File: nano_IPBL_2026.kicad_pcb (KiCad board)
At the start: 2 copper layers, 44 x 85 mm, 21 parts, among them J1 DB301V-5.0-2P, M1 Motor_Servo, M10 Motor_Servo, M11 Motor_Servo, M12 Motor_Servo, M2 Motor_Servo, M3 Motor_Servo, M4 Motor_Servo, M5 Motor_Servo, M6 Motor_Servo, M7 Motor_Servo, M8 Motor_Servo, M9 Motor_Servo

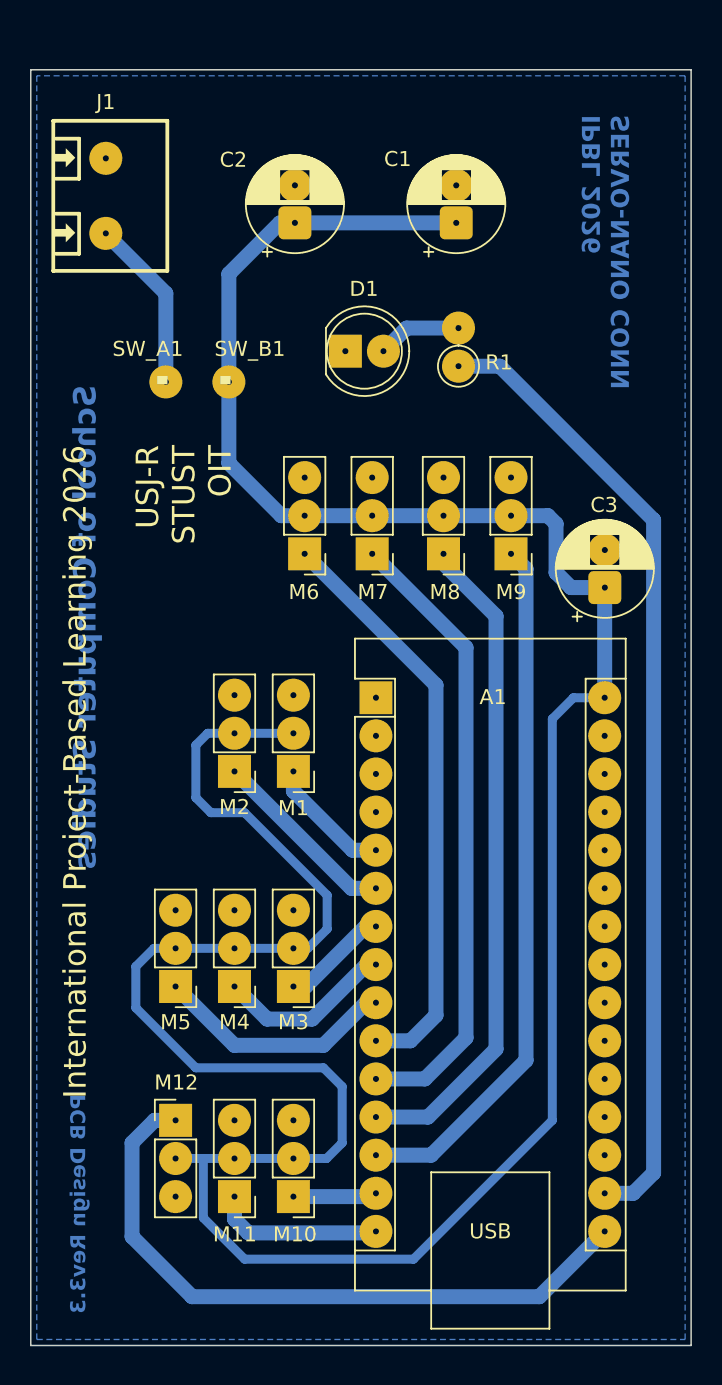
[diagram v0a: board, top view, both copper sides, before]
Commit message: Update screw terminal footprint and replace SW_A1/SW_B1 mounting holes with header
Screw terminal footprint now includes its 3D model counterpart. SW_A1
and SW_B1 mounting holes replaced with a 1-pin connected header.
Copper/silkscreen layer view colors changed from inverted to colored.
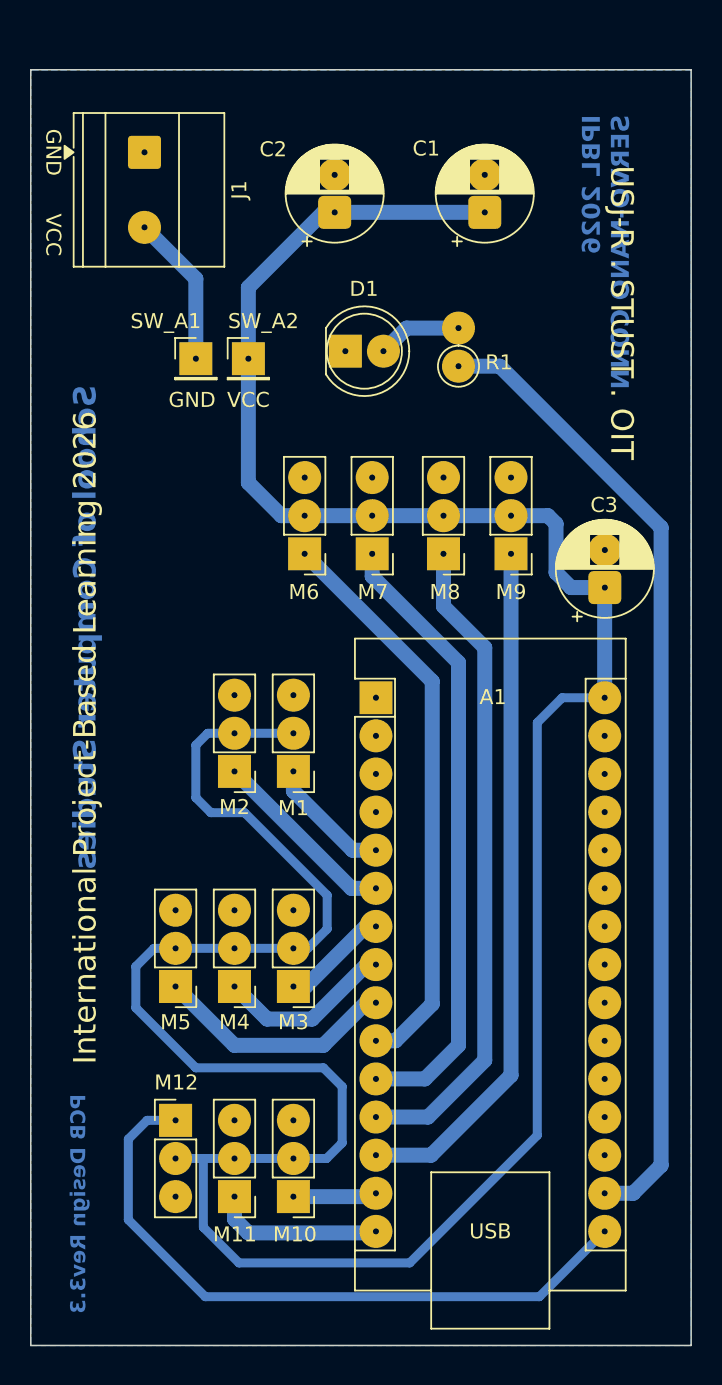
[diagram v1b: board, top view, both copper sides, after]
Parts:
- removed SW_B1: MountingHole_Pad, Arduino_MountingHole:MountingHole_1.2mm_M2_Pad_EDITED
- added SW_A2: Conn_01x01_Pin, Connector_PinHeader_2.54mm:PinHeader_1x01_P2.54mm_Vertical, F.Cu at (117.5, 69.2)
- J1: footprint lcsc:CONN-TH_2P-P5.00_L7.6-W10.0 -> TerminalBlock_Phoenix:TerminalBlock_Phoenix_MKDS-1,5-2_1x02_P5.00mm_Horizontal
- SW_A1: value MountingHole_Pad -> Conn_01x01_Pin; footprint Arduino_MountingHole:MountingHole_1.2mm_M2_Pad_EDITED -> Connector_PinHeader_2.54mm:PinHeader_1x01_P2.54mm_Vertical
- moved J1 3.88 mm to (110.6, 55.5)
- moved C2 2.74 mm to (123.2, 59.5)
- moved SW_A1 2.53 mm to (114.0, 69.2)
- moved C1 2.02 mm to (133.2, 59.5)
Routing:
- net VCC: track 11.6 -> 10.2 mm
- net /Servo_IN: track 203.2 -> 204.1 mm
- net /D10: track 46.8 -> 46.0 mm
- net /D7: track 39.1 -> 38.3 mm
- net /D9: track 44.3 -> 43.7 mm
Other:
- board text added: "GND"
- board text added: "International Project-Based Learning 2026"
- board text added: "USJ-R . STUST . OIT"
- board text added: "VCC"
- board text removed: "."
- board text removed: "International Project-Based Learning 2026 USJ-R STUST OIT"
